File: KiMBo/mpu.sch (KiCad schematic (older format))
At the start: 11 parts, among them U1 OSD3358, U4 74LVC1G74

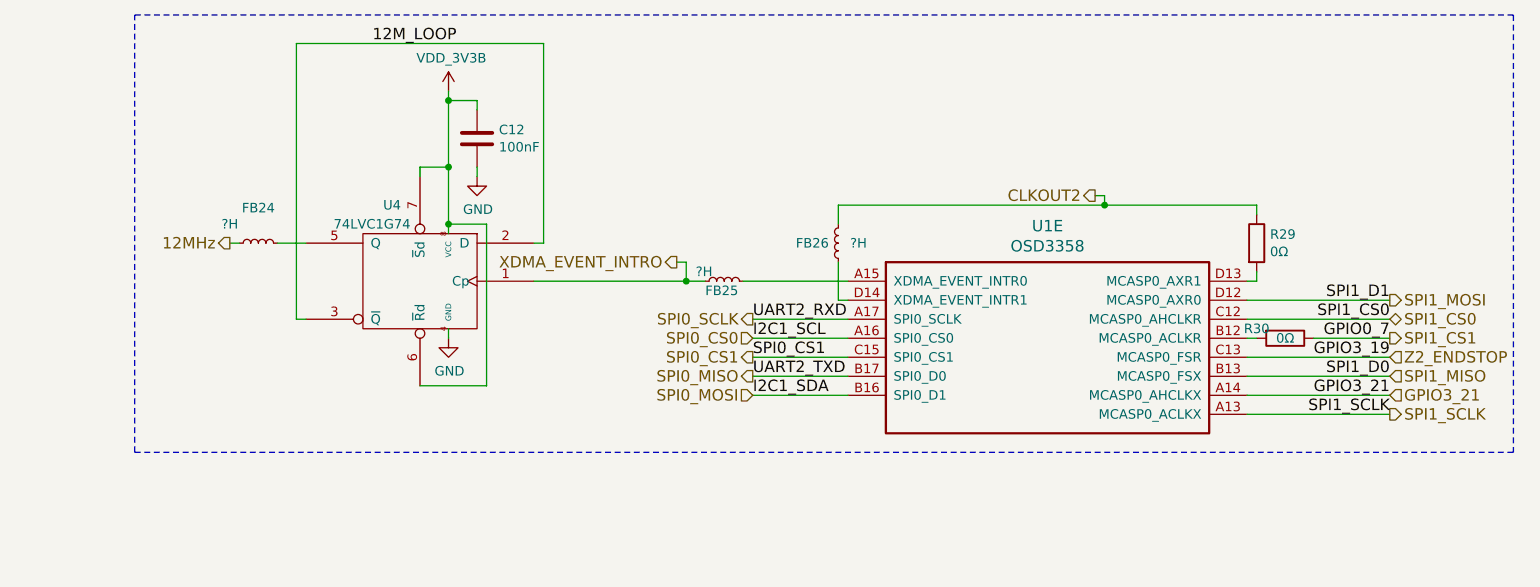
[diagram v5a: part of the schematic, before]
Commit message: More footprint association
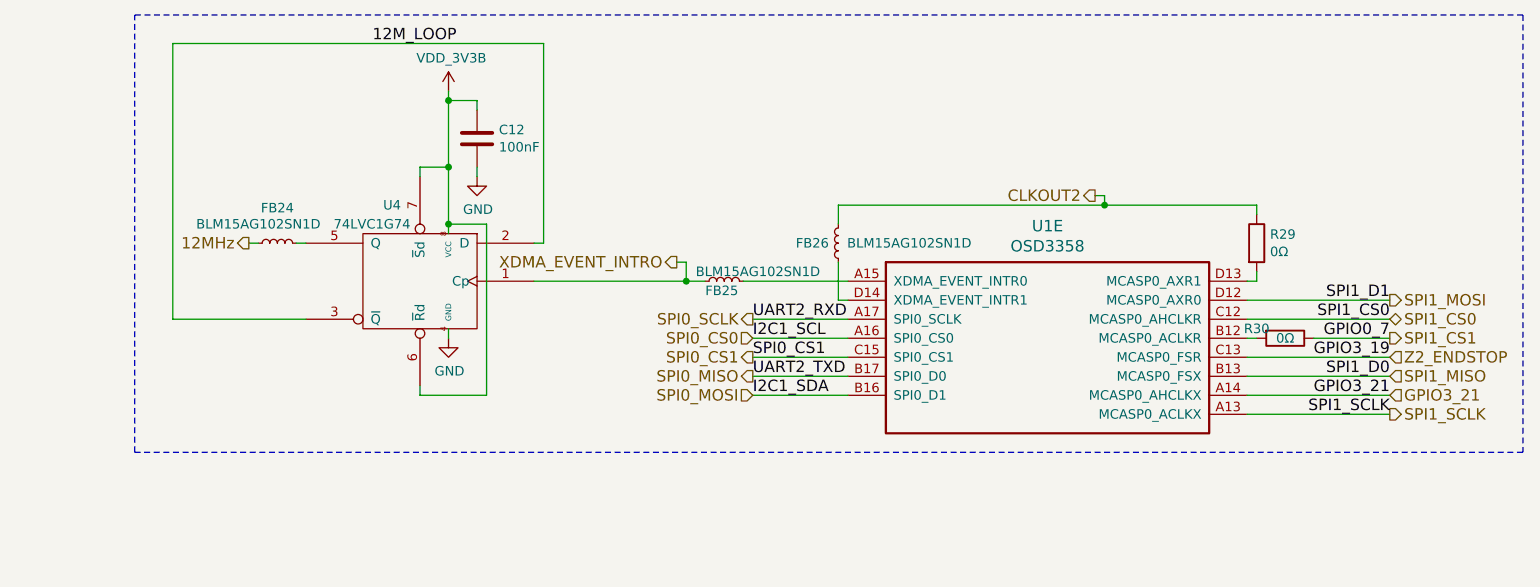
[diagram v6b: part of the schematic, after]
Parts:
- FB24, FB25, FB26: value ?H -> BLM15AG102SN1D; footprint (none) -> Resistors_SMD:R_0402
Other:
- moved on the sheet: FB24
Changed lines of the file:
@@
 $EndComp
 $Comp
-L GND #PWR084
+L GND #PWR085
 U 1 1 584B7680
 P 6100 7850
-F 0 "#PWR084" H 6100 7600 50  0001 C CNN
+F 0 "#PWR085" H 6100 7600 50  0001 C CNN
 F 1 "GND" H 6105 7677 50  0000 C CNN
 F 2 "" H 6100 7850 50  0000 C CNN
@@
 $EndComp
 $Comp
-L GND #PWR085
+L GND #PWR086
 U 1 1 584D67FE
 P 6900 4150
-F 0 "#PWR085" H 6900 3900 50  0001 C CNN
+F 0 "#PWR086" H 6900 3900 50  0001 C CNN
 F 1 "GND" H 6905 3977 50  0000 C CNN
 F 2 "" H 6900 4150 50  0000 C CNN
@@
 $EndComp
 $Comp
-L GND #PWR086
+L GND #PWR087
 U 1 1 584DD3A5
 P 7050 3300
-F 0 "#PWR086" H 7050 3050 50  0001 C CNN
+F 0 "#PWR087" H 7050 3050 50  0001 C CNN
 F 1 "GND" H 7055 3127 50  0000 C CNN
 F 2 "" H 7050 3300 50  0000 C CNN
@@
 	7350 3850 8250 3850
 Wire Wire Line
-	6150 4050 6100 4050
-Wire Wire Line
-	6100 4050 6100 2600
-Wire Wire Line
-	6100 2600 7400 2600
+	6150 4050 5450 4050
+Wire Wire Line
+	5450 4050 5450 2600
+Wire Wire Line
+	5450 2600 7400 2600
 Wire Wire Line
 	7400 2600 7400 3650
@@
 	6900 2850 6900 3600
 Wire Wire Line
-	6150 3650 6000 3650
-Wire Wire Line
-	5800 3650 5750 3650
+	6150 3650 6100 3650
+Wire Wire Line
+	5900 3650 5850 3650
 Wire Wire Line
 	6750 3300 6750 3250
@@
 Connection ~ 6900 3250
 Wire Wire Line
-	6750 4400 7100 4400
-Wire Wire Line
-	7100 4400 7100 3550
+	6750 4450 7100 4450
+Wire Wire Line
+	7100 4450 7100 3550
 Wire Wire Line
 	7100 3550 6900 3550
@@
 SPI1_CS0
 Wire Notes Line
-	5250 2450 12500 2450
-Wire Notes Line
-	12500 2450 12500 4750
-Wire Notes Line
-	12500 4750 5250 4750
+	5250 2450 12550 2450
+Wire Notes Line
+	12550 2450 12550 4750
+Wire Notes Line
+	12550 4750 5250 4750
 Wire Notes Line
 	5250 4750 5250 2450
@@
 SPI1_CS1
 $Comp
-L VDD_ADC #PWR087
+L VDD_ADC #PWR088
 U 1 1 59E85302
 P 7000 7650
-F 0 "#PWR087" H 7150 7600 50  0001 C CNN
+F 0 "#PWR088" H 7150 7600 50  0001 C CNN
 F 1 "VDD_ADC" H 7020 7793 50  0000 C CNN
 F 2 "" H 7000 7650 50  0000 C CNN
@@
 $EndComp
 $Comp
-L VDD_3V3B #PWR088
+L VDD_3V3B #PWR089
 U 1 1 59F9CAE6
 P 6900 2850
-F 0 "#PWR088" H 6900 2700 50  0001 C CNN
+F 0 "#PWR089" H 6900 2700 50  0001 C CNN
 F 1 "VDD_3V3B" H 6915 3023 50  0000 C CNN
 F 2 "" H 6900 2850 50  0000 C CNN
@@
 $EndComp
 $Comp
-L VDD_3V3B #PWR089
+L VDD_3V3B #PWR090
 U 1 1 59FC1115
 P 6100 7050
-F 0 "#PWR089" H 6100 6900 50  0001 C CNN
+F 0 "#PWR090" H 6100 6900 50  0001 C CNN
 F 1 "VDD_3V3B" H 6115 7223 50  0000 C CNN
 F 2 "" H 6100 7050 50  0000 C CNN
@@
 $EndComp
 $Comp
-L GNDA #PWR090
+L GNDA #PWR091
 U 1 1 59FCC96D
 P 7050 6500
-F 0 "#PWR090" H 7050 6250 50  0001 C CNN
+F 0 "#PWR091" H 7050 6250 50  0001 C CNN
 F 1 "GNDA" H 7055 6327 50  0000 C CNN
 F 2 "" H 7050 6500 50  0000 C CNN
@@
 Internal 150Ω FB\nfrom E8 to VSS\nunused on Replicape
 $Comp
-L PWR_FLAG #FLG091
+L PWR_FLAG #FLG092
 U 1 1 59FD3D41
 P 7150 6400
-F 0 "#FLG091" H 7150 6495 50  0001 C CNN
+F 0 "#FLG092" H 7150 6495 50  0001 C CNN
 F 1 "PWR_FLAG" H 7150 6624 50  0000 C CNN
 F 2 "" H 7150 6400 50  0000 C CNN
@@
 L INDUCTOR_Small FB24
 U 1 1 5B034EFC
-P 5900 3650
-F 0 "FB24" V 6085 3650 50  0000 C CNN
-F 1 "?H" V 6000 3800 50  0000 C CNN
-F 2 "" H 5900 3650 50  0001 C CNN
-F 3 "" H 5900 3650 50  0000 C CNN
-	1    5900 3650
+P 6000 3650
+F 0 "FB24" V 6185 3650 50  0000 C CNN
+F 1 "BLM15AG102SN1D" V 6100 3750 50  0000 C CNN
+F 2 "Resistors_SMD:R_0402" H 6000 3650 50  0001 C CNN
+F 3 "" H 6000 3650 50  0000 C CNN
+	1    6000 3650
 	0    -1   -1   0
 $EndComp
@@
 Wire Wire Line
 	8500 4050 9000 4050
-Text HLabel 5750 3650 0    60   Output ~ 0
+Text HLabel 5850 3650 0    60   Output ~ 0
 12MHz
 $Comp
@@
 P 8950 3650
 F 0 "FB26" H 9000 3650 50  0000 L CNN
-F 1 "?H" H 8800 3650 50  0000 L CNN
-F 2 "" H 8950 3650 50  0001 C CNN
+F 1 "BLM15AG102SN1D" H 8250 3650 50  0000 L CNN
+F 2 "Resistors_SMD:R_0402" H 8950 3650 50  0001 C CNN
 F 3 "" H 8950 3650 50  0000 C CNN
 	1    8950 3650
@@
 P 8350 3850
 F 0 "FB25" V 8300 3750 50  0000 L CNN
-F 1 "?H" V 8400 3700 50  0000 L CNN
-F 2 "" H 8350 3850 50  0001 C CNN
+F 1 "BLM15AG102SN1D" V 8400 3700 50  0000 L CNN
+F 2 "Resistors_SMD:R_0402" H 8350 3850 50  0001 C CNN
 F 3 "" H 8350 3850 50  0000 C CNN
 	1    8350 3850
@@
 Text HLabel 8500 4150 0    60   Input ~ 0
 SPI0_CS0
+Wire Wire Line
+	6750 4400 6750 4450
 $EndSCHEMATC

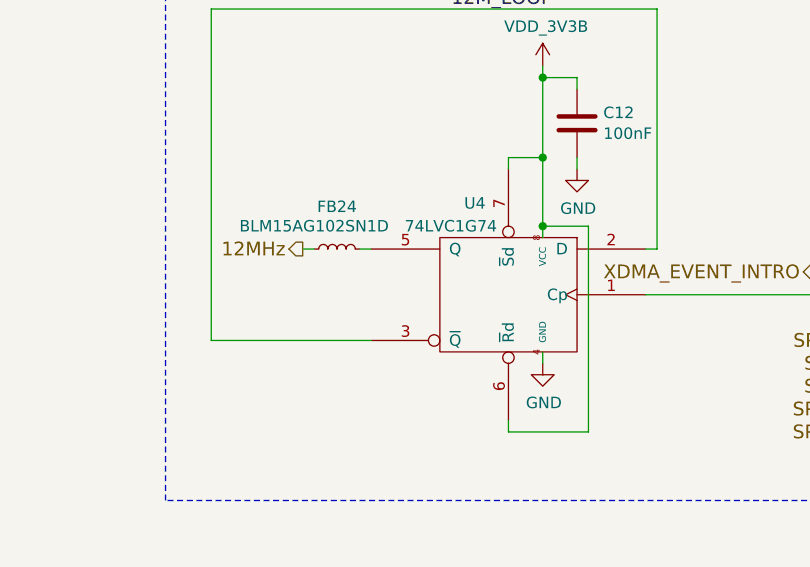
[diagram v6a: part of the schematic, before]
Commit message: Create more footprints and add more associations
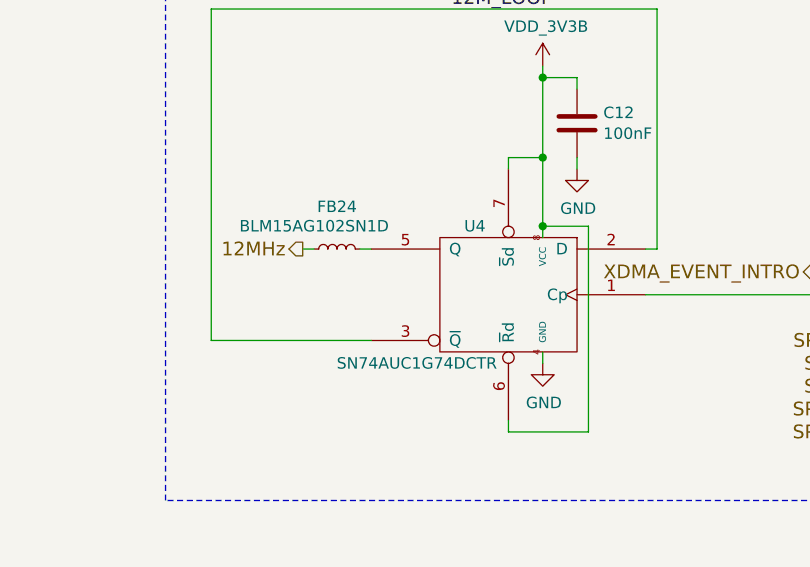
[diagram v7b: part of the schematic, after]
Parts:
- U4: value 74LVC1G74 -> SN74AUC1G74DCTR; footprint (none) -> KiMBo:DCT-MSOP-8_3x3mm_Pitch0.65mm
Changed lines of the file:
@@
 U 1 1 584D5286
 P 6750 3850
-F 0 "U4" H 6850 4250 50  0000 L CNN
-F 1 "74LVC1G74" H 6800 4150 50  0000 L CNN
-F 2 "" H 6750 3850 50  0001 C CNN
+F 0 "U4" H 6850 4150 50  0000 L CNN
+F 1 "SN74AUC1G74DCTR" H 6800 3550 50  0000 L CNN
+F 2 "KiMBo:DCT-MSOP-8_3x3mm_Pitch0.65mm" H 6750 3850 50  0001 C CNN
 F 3 "" H 6750 3850 50  0000 C CNN
 	1    6750 3850

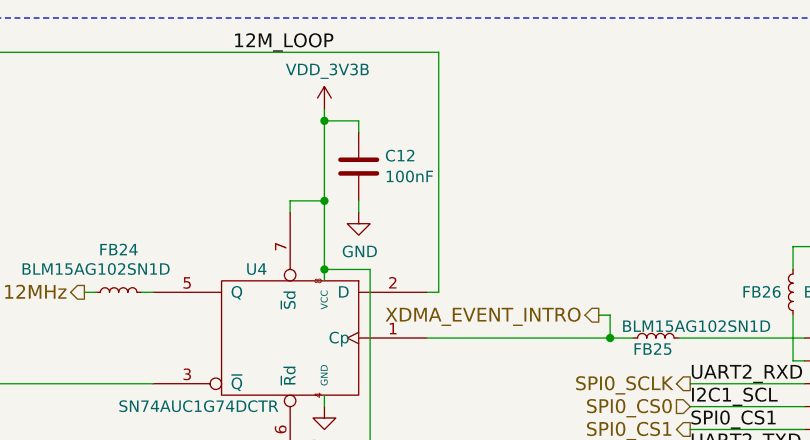
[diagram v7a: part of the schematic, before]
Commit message: Begin layout
Arrange all connectors to get a feel for the area.
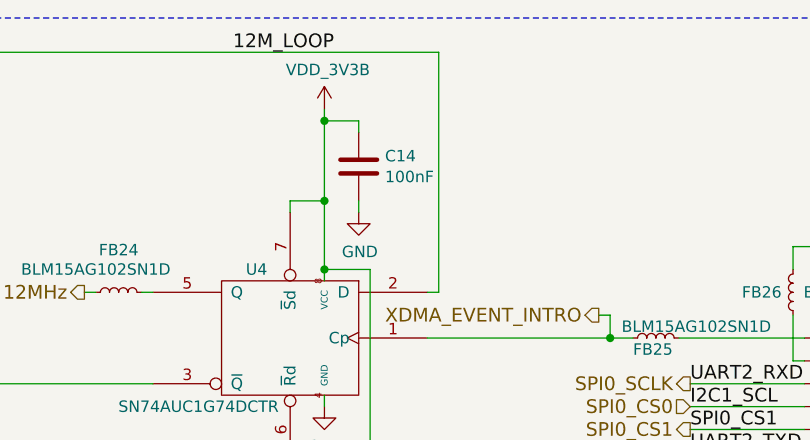
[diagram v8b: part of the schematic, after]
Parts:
- renumbered C12 to C14
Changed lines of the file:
@@
 $EndComp
 $Comp
-L GND #PWR085
+L GND #PWR088
 U 1 1 584B7680
 P 6100 7850
-F 0 "#PWR085" H 6100 7600 50  0001 C CNN
+F 0 "#PWR088" H 6100 7600 50  0001 C CNN
 F 1 "GND" H 6105 7677 50  0000 C CNN
 F 2 "" H 6100 7850 50  0000 C CNN
@@
 $EndComp
 $Comp
-L GND #PWR086
+L GND #PWR089
 U 1 1 584D67FE
 P 6900 4150
-F 0 "#PWR086" H 6900 3900 50  0001 C CNN
+F 0 "#PWR089" H 6900 3900 50  0001 C CNN
 F 1 "GND" H 6905 3977 50  0000 C CNN
 F 2 "" H 6900 4150 50  0000 C CNN
@@
 $EndComp
 $Comp
-L GND #PWR087
+L GND #PWR090
 U 1 1 584DD3A5
 P 7050 3300
-F 0 "#PWR087" H 7050 3050 50  0001 C CNN
+F 0 "#PWR090" H 7050 3050 50  0001 C CNN
 F 1 "GND" H 7055 3127 50  0000 C CNN
 F 2 "" H 7050 3300 50  0000 C CNN
@@
 SPI1_CS1
 $Comp
-L VDD_ADC #PWR088
+L VDD_ADC #PWR091
 U 1 1 59E85302
 P 7000 7650
-F 0 "#PWR088" H 7150 7600 50  0001 C CNN
+F 0 "#PWR091" H 7150 7600 50  0001 C CNN
 F 1 "VDD_ADC" H 7020 7793 50  0000 C CNN
 F 2 "" H 7000 7650 50  0000 C CNN
@@
 $EndComp
 $Comp
-L VDD_3V3B #PWR089
+L VDD_3V3B #PWR092
 U 1 1 59F9CAE6
 P 6900 2850
-F 0 "#PWR089" H 6900 2700 50  0001 C CNN
+F 0 "#PWR092" H 6900 2700 50  0001 C CNN
 F 1 "VDD_3V3B" H 6915 3023 50  0000 C CNN
 F 2 "" H 6900 2850 50  0000 C CNN
@@
 $EndComp
 $Comp
-L VDD_3V3B #PWR090
+L VDD_3V3B #PWR093
 U 1 1 59FC1115
 P 6100 7050
-F 0 "#PWR090" H 6100 6900 50  0001 C CNN
+F 0 "#PWR093" H 6100 6900 50  0001 C CNN
 F 1 "VDD_3V3B" H 6115 7223 50  0000 C CNN
 F 2 "" H 6100 7050 50  0000 C CNN
@@
 $EndComp
 $Comp
-L GNDA #PWR091
+L GNDA #PWR094
 U 1 1 59FCC96D
 P 7050 6500
-F 0 "#PWR091" H 7050 6250 50  0001 C CNN
+F 0 "#PWR094" H 7050 6250 50  0001 C CNN
 F 1 "GNDA" H 7055 6327 50  0000 C CNN
 F 2 "" H 7050 6500 50  0000 C CNN
@@
 Internal 150Ω FB\nfrom E8 to VSS\nunused on Replicape
 $Comp
-L PWR_FLAG #FLG092
+L PWR_FLAG #FLG095
 U 1 1 59FD3D41
 P 7150 6400
-F 0 "#FLG092" H 7150 6495 50  0001 C CNN
+F 0 "#FLG095" H 7150 6495 50  0001 C CNN
 F 1 "PWR_FLAG" H 7150 6624 50  0000 C CNN
 F 2 "" H 7150 6400 50  0000 C CNN
@@
 $EndComp
 $Comp
-L C C12
+L C C14
 U 1 1 58EAE0AA
 P 7050 3100
-F 0 "C12" H 7165 3146 50  0000 L CNN
+F 0 "C14" H 7165 3146 50  0000 L CNN
 F 1 "100nF" H 7165 3055 50  0000 L CNN
 F 2 "Capacitors_SMD:C_0603" H 7088 2950 50  0001 C CNN
